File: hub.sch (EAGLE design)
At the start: 50 parts, among them U1 LM3526-L, X1 12MHz

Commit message: pick resistors
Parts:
- R1, R21, R24: DIGIKEY (none) -> 311-10.0KCRCT-ND; MPN (none) -> RC0805FR-0710KL; OC_MOUSER (none) -> 603-RC0805FR-0710KL
- R16: DIGIKEY (none) -> 311-47.0KCRCT-ND; MPN (none) -> RC0805FR-0747KL; OC_MOUSER (none) -> 603-RC0805FR-0747KL
- R2, R22, R23: DIGIKEY (none) -> 311-100KCRCT-ND; MPN (none) -> RC0805FR-07100KL; OC_MOUSER (none) -> 603-RC0805FR-07100KL
- R3: DIGIKEY (none) -> P649HCT-ND; MPN (none) -> ERJ-6ENF6490V; OC_MOUSER (none) -> 667-ERJ-6ENF6490V
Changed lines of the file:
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@@
 </part>
 <part name="SUPPLY1" library="supply2" library_urn="urn:adsk.eagle:library:372" deviceset="GND" device=""/>
-<part name="R1" library="rcl" library_urn="urn:adsk.eagle:library:334" deviceset="R-US_" device="M0805" package3d_urn="urn:adsk.eagle:package:23556/1" value="10K"/>
+<part name="R1" library="rcl" library_urn="urn:adsk.eagle:library:334" deviceset="R-US_" device="M0805" package3d_urn="urn:adsk.eagle:package:23556/1" value="10K">
+<attribute name="DIGIKEY" value="311-10.0KCRCT-ND"/>
+<attribute name="MPN" value="RC0805FR-0710KL"/>
+<attribute name="OC_MOUSER" value="603-RC0805FR-0710KL"/>
+</part>
 <part name="C13" library="rcl" library_urn="urn:adsk.eagle:library:334" deviceset="C-EU" device="C0805" package3d_urn="urn:adsk.eagle:package:23617/2" value="1uF"/>
-<part name="R16" library="rcl" library_urn="urn:adsk.eagle:library:334" deviceset="R-US_" device="M0805" package3d_urn="urn:adsk.eagle:package:23556/1" value="47K"/>
+<part name="R16" library="rcl" library_urn="urn:adsk.eagle:library:334" deviceset="R-US_" device="M0805" package3d_urn="urn:adsk.eagle:package:23556/1" value="47K">
+<attribute name="DIGIKEY" value="311-47.0KCRCT-ND"/>
+<attribute name="MPN" value="RC0805FR-0747KL"/>
+<attribute name="OC_MOUSER" value="603-RC0805FR-0747KL"/>
+</part>
 <part name="SUPPLY2" library="supply2" library_urn="urn:adsk.eagle:library:372" deviceset="GND" device=""/>
-<part name="R2" library="rcl" library_urn="urn:adsk.eagle:library:334" deviceset="R-US_" device="M0805" package3d_urn="urn:adsk.eagle:package:23556/1" value="100K"/>
+<part name="R2" library="rcl" library_urn="urn:adsk.eagle:library:334" deviceset="R-US_" device="M0805" package3d_urn="urn:adsk.eagle:package:23556/1" value="100K">
+<attribute name="DIGIKEY" value="311-100KCRCT-ND"/>
+<attribute name="MPN" value="RC0805FR-07100KL"/>
+<attribute name="OC_MOUSER" value="603-RC0805FR-07100KL"/>
+</part>
 <part name="SUPPLY3" library="supply2" library_urn="urn:adsk.eagle:library:372" deviceset="GND" device=""/>
-<part name="R3" library="rcl" library_urn="urn:adsk.eagle:library:334" deviceset="R-US_" device="M0805" package3d_urn="urn:adsk.eagle:package:23556/1" value="650R 1%"/>
+<part name="R3" library="rcl" library_urn="urn:adsk.eagle:library:334" deviceset="R-US_" device="M0805" package3d_urn="urn:adsk.eagle:package:23556/1" value="650R 1%">
+<attribute name="DIGIKEY" value="P649HCT-ND"/>
+<attribute name="MPN" value="ERJ-6ENF6490V"/>
+<attribute name="OC_MOUSER" value="667-ERJ-6ENF6490V"/>
+</part>
 <part name="SUPPLY4" library="supply2" library_urn="urn:adsk.eagle:library:372" deviceset="GND" device=""/>
 <part name="C14" library="rcl" library_urn="urn:adsk.eagle:library:334" deviceset="C-EU" device="C0805" package3d_urn="urn:adsk.eagle:package:23617/2" value="18P">
@@
 <part name="C17" library="rcl" library_urn="urn:adsk.eagle:library:334" deviceset="C-EU" device="C0805" package3d_urn="urn:adsk.eagle:package:23617/2" value="0.1uF"/>
 <part name="SUPPLY20" library="supply2" library_urn="urn:adsk.eagle:library:372" deviceset="GND" device=""/>
-<part name="R21" library="rcl" library_urn="urn:adsk.eagle:library:334" deviceset="R-US_" device="M0805" package3d_urn="urn:adsk.eagle:package:23556/1" value="10K"/>
-<part name="R22" library="rcl" library_urn="urn:adsk.eagle:library:334" deviceset="R-US_" device="M0805" package3d_urn="urn:adsk.eagle:package:23556/1" value="100K"/>
-<part name="R23" library="rcl" library_urn="urn:adsk.eagle:library:334" deviceset="R-US_" device="M0805" package3d_urn="urn:adsk.eagle:package:23556/1" value="100K"/>
-<part name="R24" library="rcl" library_urn="urn:adsk.eagle:library:334" deviceset="R-US_" device="M0805" package3d_urn="urn:adsk.eagle:package:23556/1" value="10K"/>
+<part name="R21" library="rcl" library_urn="urn:adsk.eagle:library:334" deviceset="R-US_" device="M0805" package3d_urn="urn:adsk.eagle:package:23556/1" value="10K">
+<attribute name="DIGIKEY" value="311-10.0KCRCT-ND"/>
+<attribute name="MPN" value="RC0805FR-0710KL"/>
+<attribute name="OC_MOUSER" value="603-RC0805FR-0710KL"/>
+</part>
+<part name="R22" library="rcl" library_urn="urn:adsk.eagle:library:334" deviceset="R-US_" device="M0805" package3d_urn="urn:adsk.eagle:package:23556/1" value="100K">
+<attribute name="DIGIKEY" value="311-100KCRCT-ND"/>
+<attribute name="MPN" value="RC0805FR-07100KL"/>
+<attribute name="OC_MOUSER" value="603-RC0805FR-07100KL"/>
+</part>
+<part name="R23" library="rcl" library_urn="urn:adsk.eagle:library:334" deviceset="R-US_" device="M0805" package3d_urn="urn:adsk.eagle:package:23556/1" value="100K">
+<attribute name="DIGIKEY" value="311-100KCRCT-ND"/>
+<attribute name="MPN" value="RC0805FR-07100KL"/>
+<attribute name="OC_MOUSER" value="603-RC0805FR-07100KL"/>
+</part>
+<part name="R24" library="rcl" library_urn="urn:adsk.eagle:library:334" deviceset="R-US_" device="M0805" package3d_urn="urn:adsk.eagle:package:23556/1" value="10K">
+<attribute name="DIGIKEY" value="311-10.0KCRCT-ND"/>
+<attribute name="MPN" value="RC0805FR-0710KL"/>
+<attribute name="OC_MOUSER" value="603-RC0805FR-0710KL"/>
+</part>
 <part name="TSUP3" library="sn65220_40" deviceset="SN65220" device="DBV">
 <attribute name="DIGIKEY" value="296-9694-1-ND"/>
@@
 </instance>
 <instance part="SUPPLY1" gate="GND" x="-15.24" y="-55.88"/>
-<instance part="R1" gate="G$1" x="66.04" y="-35.56" rot="R90"/>
+<instance part="R1" gate="G$1" x="66.04" y="-35.56" rot="R90">
+<attribute name="DIGIKEY" x="66.04" y="-35.56" size="1.778" layer="96" rot="R90" display="off"/>
+<attribute name="MPN" x="66.04" y="-35.56" size="1.778" layer="96" rot="R90" display="off"/>
+<attribute name="OC_MOUSER" x="66.04" y="-35.56" size="1.778" layer="96" rot="R90" display="off"/>
+</instance>
 <instance part="C13" gate="G$1" x="66.04" y="-53.34"/>
-<instance part="R16" gate="G$1" x="78.74" y="-55.88" rot="R90"/>
+<instance part="R16" gate="G$1" x="78.74" y="-55.88" rot="R90">
+<attribute name="DIGIKEY" x="78.74" y="-55.88" size="1.778" layer="96" rot="R90" display="off"/>
+<attribute name="MPN" x="78.74" y="-55.88" size="1.778" layer="96" rot="R90" display="off"/>
+<attribute name="OC_MOUSER" x="78.74" y="-55.88" size="1.778" layer="96" rot="R90" display="off"/>
+</instance>
 <instance part="SUPPLY2" gate="GND" x="66.04" y="-71.12"/>
-<instance part="R2" gate="G$1" x="101.6" y="-50.8"/>
+<instance part="R2" gate="G$1" x="101.6" y="-50.8">
+<attribute name="DIGIKEY" x="101.6" y="-50.8" size="1.778" layer="96" display="off"/>
+<attribute name="MPN" x="101.6" y="-50.8" size="1.778" layer="96" display="off"/>
+<attribute name="OC_MOUSER" x="101.6" y="-50.8" size="1.778" layer="96" display="off"/>
+</instance>
 <instance part="SUPPLY3" gate="GND" x="109.22" y="-60.96"/>
-<instance part="R3" gate="G$1" x="129.54" y="-45.72" rot="R90"/>
+<instance part="R3" gate="G$1" x="129.54" y="-45.72" rot="R90">
+<attribute name="DIGIKEY" x="129.54" y="-45.72" size="1.778" layer="96" rot="R90" display="off"/>
+<attribute name="MPN" x="129.54" y="-45.72" size="1.778" layer="96" rot="R90" display="off"/>
+<attribute name="OC_MOUSER" x="129.54" y="-45.72" size="1.778" layer="96" rot="R90" display="off"/>
+</instance>
 <instance part="SUPPLY4" gate="GND" x="129.54" y="-68.58"/>
 <instance part="C14" gate="G$1" x="157.48" y="-53.34">
@@
 <instance part="C17" gate="G$1" x="48.26" y="-86.36"/>
 <instance part="SUPPLY20" gate="GND" x="48.26" y="-99.06"/>
-<instance part="R21" gate="G$1" x="-43.18" y="-71.12" rot="R90"/>
-<instance part="R22" gate="G$1" x="-33.02" y="-71.12" rot="R90"/>
-<instance part="R23" gate="G$1" x="-22.86" y="-71.12" rot="R90"/>
-<instance part="R24" gate="G$1" x="-12.7" y="-71.12" rot="R90"/>
+<instance part="R21" gate="G$1" x="-43.18" y="-71.12" rot="R90">
+<attribute name="OC_MOUSER" x="-43.18" y="-71.12" size="1.778" layer="96" rot="R90" display="off"/>
+<attribute name="DIGIKEY" x="-43.18" y="-71.12" size="1.778" layer="96" rot="R90" display="off"/>
+<attribute name="MPN" x="-43.18" y="-71.12" size="1.778" layer="96" rot="R90" display="off"/>
+</instance>
+<instance part="R22" gate="G$1" x="-33.02" y="-71.12" rot="R90">
+<attribute name="MPN" x="-33.02" y="-71.12" size="1.778" layer="96" rot="R90" display="off"/>
+<attribute name="DIGIKEY" x="-33.02" y="-71.12" size="1.778" layer="96" rot="R90" display="off"/>
+<attribute name="OC_MOUSER" x="-33.02" y="-71.12" size="1.778" layer="96" rot="R90" display="off"/>
+</instance>
+<instance part="R23" gate="G$1" x="-22.86" y="-71.12" rot="R90">
+<attribute name="MPN" x="-22.86" y="-71.12" size="1.778" layer="96" rot="R90" display="off"/>
+<attribute name="DIGIKEY" x="-22.86" y="-71.12" size="1.778" layer="96" rot="R90" display="off"/>
+<attribute name="OC_MOUSER" x="-22.86" y="-71.12" size="1.778" layer="96" rot="R90" display="off"/>
+</instance>
+<instance part="R24" gate="G$1" x="-12.7" y="-71.12" rot="R90">
+<attribute name="OC_MOUSER" x="-12.7" y="-71.12" size="1.778" layer="96" rot="R90" display="off"/>
+<attribute name="DIGIKEY" x="-12.7" y="-71.12" size="1.778" layer="96" rot="R90" display="off"/>
+<attribute name="MPN" x="-12.7" y="-71.12" size="1.778" layer="96" rot="R90" display="off"/>
+</instance>
 <instance part="TSUP3" gate="G$1" x="45.72" y="53.34" rot="R90">
 <attribute name="DIGIKEY" x="45.72" y="53.34" size="1.778" layer="96" rot="R90" display="off"/>

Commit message: pick capacitors
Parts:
- C1, C10, C11, C12, C16, C17, C19, C20, C21, C22, C4, C8, C9: DIGIKEY (none) -> 490-1666-1-ND; MPN (none) -> GRM21BR71H104KA01L; OC_MOUSER (none) -> 81-GRM40X104K50L
- C13, C2, C3, C5: DIGIKEY (none) -> 399-1284-1-ND; MPN (none) -> C0805C105K4RACTU; OC_MOUSER (none) -> 80-C0805C105K4R

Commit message: complete BOM
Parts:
- C14, C15: MPN (none) -> CL10C180JB8NNNC
- LB1, LB6: value (none) -> 220; DIGIKEY (none) -> 490-1054-1-ND; MPN (none) -> BLM21PG221SN1D; OC_MOUSER (none) -> 81-BLM21P221SG
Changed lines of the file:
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@@
 <part name="C14" library="rcl" library_urn="urn:adsk.eagle:library:334" deviceset="C-EU" device="C0805" package3d_urn="urn:adsk.eagle:package:23617/2" value="18P">
 <attribute name="DIGIKEY" value="1276-1089-1-ND"/>
+<attribute name="MPN" value="CL10C180JB8NNNC"/>
 <attribute name="OC_MOUSER" value="77-VJ0603A180JXACBC"/>
 </part>
 <part name="C15" library="rcl" library_urn="urn:adsk.eagle:library:334" deviceset="C-EU" device="C0805" package3d_urn="urn:adsk.eagle:package:23617/2" value="18P">
 <attribute name="DIGIKEY" value="1276-1089-1-ND"/>
+<attribute name="MPN" value="CL10C180JB8NNNC"/>
 <attribute name="OC_MOUSER" value="77-VJ0603A180JXACBC"/>
 </part>
@@
 <part name="SUPPLY23" library="supply2" library_urn="urn:adsk.eagle:library:372" deviceset="GND" device=""/>
 <part name="SUPPLY24" library="supply2" library_urn="urn:adsk.eagle:library:372" deviceset="GND" device=""/>
-<part name="LB1" library="rcl" library_urn="urn:adsk.eagle:library:334" deviceset="R-EU_" device="R0805" package3d_urn="urn:adsk.eagle:package:23553/2"/>
+<part name="LB1" library="rcl" library_urn="urn:adsk.eagle:library:334" deviceset="R-EU_" device="R0805" package3d_urn="urn:adsk.eagle:package:23553/2" value="220">
+<attribute name="DIGIKEY" value="490-1054-1-ND"/>
+<attribute name="MPN" value="BLM21PG221SN1D"/>
+<attribute name="OC_MOUSER" value="81-BLM21P221SG"/>
+</part>
 <part name="+3V3_1" library="supply1" library_urn="urn:adsk.eagle:library:371" deviceset="+3V3" device=""/>
 <part name="+3V3_4" library="supply1" library_urn="urn:adsk.eagle:library:371" deviceset="+3V3" device=""/>
@@
 <part name="P+1" library="supply1" library_urn="urn:adsk.eagle:library:371" deviceset="V+" device=""/>
 <part name="P+2" library="supply1" library_urn="urn:adsk.eagle:library:371" deviceset="V+" device=""/>
-<part name="LB6" library="rcl" library_urn="urn:adsk.eagle:library:334" deviceset="R-EU_" device="R0805" package3d_urn="urn:adsk.eagle:package:23553/2"/>
+<part name="LB6" library="rcl" library_urn="urn:adsk.eagle:library:334" deviceset="R-EU_" device="R0805" package3d_urn="urn:adsk.eagle:package:23553/2" value="220">
+<attribute name="DIGIKEY" value="490-1054-1-ND"/>
+<attribute name="MPN" value="BLM21PG221SN1D"/>
+<attribute name="OC_MOUSER" value="81-BLM21P221SG"/>
+</part>
 <part name="SUPPLY26" library="supply2" library_urn="urn:adsk.eagle:library:372" deviceset="GND" device=""/>
 <part name="J3" library="InputOutputIO (rev17e)" deviceset="61400826021" device="">
@@
 <attribute name="DIGIKEY" x="157.48" y="-53.34" size="1.778" layer="96" display="off"/>
 <attribute name="OC_MOUSER" x="157.48" y="-53.34" size="1.778" layer="96" display="off"/>
+<attribute name="MPN" x="157.48" y="-53.34" size="1.778" layer="96" display="off"/>
 </instance>
 <instance part="C15" gate="G$1" x="193.04" y="-53.34">
 <attribute name="DIGIKEY" x="193.04" y="-53.34" size="1.778" layer="96" display="off"/>
 <attribute name="OC_MOUSER" x="193.04" y="-53.34" size="1.778" layer="96" display="off"/>
+<attribute name="MPN" x="193.04" y="-53.34" size="1.778" layer="96" display="off"/>
 </instance>
 <instance part="SUPPLY5" gate="GND" x="157.48" y="-68.58"/>
@@
 <instance part="SUPPLY23" gate="GND" x="43.18" y="40.64"/>
 <instance part="SUPPLY24" gate="GND" x="38.1" y="73.66"/>
-<instance part="LB1" gate="G$1" x="63.5" y="73.66"/>
+<instance part="LB1" gate="G$1" x="63.5" y="73.66">
+<attribute name="MPN" x="63.5" y="73.66" size="1.778" layer="96" display="off"/>
+<attribute name="DIGIKEY" x="63.5" y="73.66" size="1.778" layer="96" display="off"/>
+<attribute name="OC_MOUSER" x="63.5" y="73.66" size="1.778" layer="96" display="off"/>
+</instance>
 <instance part="+3V3_1" gate="G$1" x="68.58" y="48.26"/>
 <instance part="+3V3_4" gate="G$1" x="149.86" y="93.98"/>
@@
 <instance part="P+1" gate="1" x="86.36" y="48.26"/>
 <instance part="P+2" gate="1" x="114.3" y="48.26"/>
-<instance part="LB6" gate="G$1" x="78.74" y="30.48"/>
+<instance part="LB6" gate="G$1" x="78.74" y="30.48">
+<attribute name="MPN" x="78.74" y="30.48" size="1.778" layer="96" display="off"/>
+<attribute name="DIGIKEY" x="78.74" y="30.48" size="1.778" layer="96" display="off"/>
+<attribute name="OC_MOUSER" x="78.74" y="30.48" size="1.778" layer="96" display="off"/>
+</instance>
 <instance part="SUPPLY26" gate="GND" x="48.26" y="-10.16" rot="R90"/>
 <instance part="J3" gate="G$1" x="236.22" y="-48.26" rot="R270">

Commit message: finish pin-strapping
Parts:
- added R5, R6: 10K, rcl:R-US_M0805
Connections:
- removed net NOVRP3: U$1.OVR#[3]
- removed net NOVRP4: U$1.OVR#[4]
- new net N$6: R6.2, U$1.GREEN[4]
- new net N$7: R5.2, U$1.GREEN[3]
- net +3V3: now also R5.1, R6.1, U$1.OVR#[3], U$1.OVR#[4]

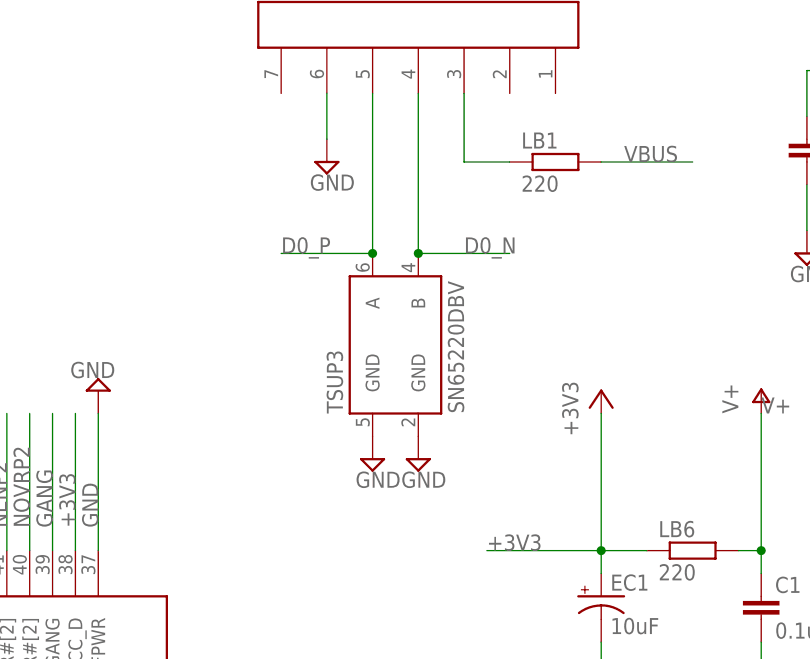
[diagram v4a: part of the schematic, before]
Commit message: re-route USB for oshpark PCBs
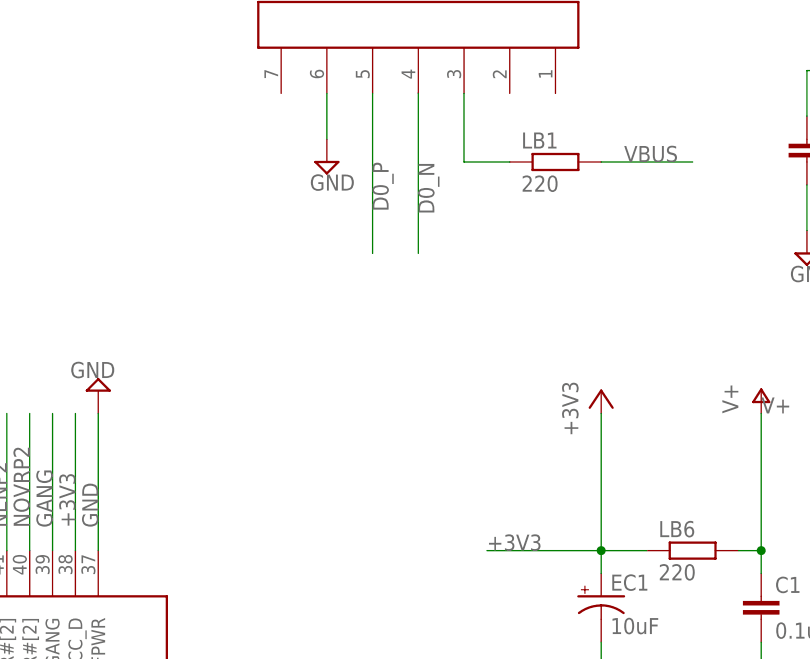
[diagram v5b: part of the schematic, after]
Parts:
- removed TSUP3: SN65220DBV, sn65220_40:SN65220DBV
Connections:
- net D0_N: no longer TSUP3.B
- net D0_P: no longer TSUP3.A
- net GND: no longer TSUP3.GND@1, TSUP3.GND@2
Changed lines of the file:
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@@
 <attribute name="OC_MOUSER" value="603-RC0805FR-0710KL"/>
 </part>
-<part name="TSUP3" library="sn65220_40" deviceset="SN65220" device="DBV">
-<attribute name="DIGIKEY" value="296-9694-1-ND"/>
-<attribute name="MPN" value="SN65220DBVR"/>
-<attribute name="OC_MOUSER" value="595-SN65220DBVR"/>
-</part>
-<part name="SUPPLY22" library="supply2" library_urn="urn:adsk.eagle:library:372" deviceset="GND" device=""/>
-<part name="SUPPLY23" library="supply2" library_urn="urn:adsk.eagle:library:372" deviceset="GND" device=""/>
 <part name="SUPPLY24" library="supply2" library_urn="urn:adsk.eagle:library:372" deviceset="GND" device=""/>
 <part name="LB1" library="rcl" library_urn="urn:adsk.eagle:library:334" deviceset="R-EU_" device="R0805" package3d_urn="urn:adsk.eagle:package:23553/2" value="220">
@@
 <attribute name="MPN" x="-12.7" y="-71.12" size="1.778" layer="96" rot="R90" display="off"/>
 </instance>
-<instance part="TSUP3" gate="G$1" x="45.72" y="53.34" rot="R90">
-<attribute name="DIGIKEY" x="45.72" y="53.34" size="1.778" layer="96" rot="R90" display="off"/>
-<attribute name="MPN" x="45.72" y="53.34" size="1.778" layer="96" rot="R90" display="off"/>
-<attribute name="OC_MOUSER" x="45.72" y="53.34" size="1.778" layer="96" rot="R90" display="off"/>
-</instance>
-<instance part="SUPPLY22" gate="GND" x="48.26" y="40.64"/>
-<instance part="SUPPLY23" gate="GND" x="43.18" y="40.64"/>
 <instance part="SUPPLY24" gate="GND" x="38.1" y="73.66"/>
 <instance part="LB1" gate="G$1" x="63.5" y="73.66">
@@
 </segment>
 <segment>
-<pinref part="TSUP3" gate="G$1" pin="GND@2"/>
-<pinref part="SUPPLY22" gate="GND" pin="GND"/>
-</segment>
-<segment>
-<pinref part="TSUP3" gate="G$1" pin="GND@1"/>
-<pinref part="SUPPLY23" gate="GND" pin="GND"/>
-</segment>
-<segment>
 <pinref part="U$1" gate="G$1" pin="SELFPWR"/>
 <wire x1="12.7" y1="30.48" x2="12.7" y2="45.72" width="0.1524" layer="91"/>
@@
 </segment>
 <segment>
-<pinref part="TSUP3" gate="G$1" pin="B"/>
-<wire x1="48.26" y1="63.5" x2="58.42" y2="63.5" width="0.1524" layer="91"/>
-<label x="53.34" y="63.5" size="1.778" layer="95"/>
+<label x="48.26" y="73.66" size="1.778" layer="95" rot="R270"/>
 <pinref part="J2" gate="G$1" pin="4"/>
 <wire x1="48.26" y1="81.28" x2="48.26" y2="63.5" width="0.1524" layer="91"/>
-<junction x="48.26" y="63.5"/>
 </segment>
 </net>
@@
 </segment>
 <segment>
-<pinref part="TSUP3" gate="G$1" pin="A"/>
-<wire x1="43.18" y1="63.5" x2="33.02" y2="63.5" width="0.1524" layer="91"/>
-<label x="33.02" y="63.5" size="1.778" layer="95"/>
+<label x="43.18" y="73.66" size="1.778" layer="95" rot="R270"/>
 <pinref part="J2" gate="G$1" pin="5"/>
 <wire x1="43.18" y1="81.28" x2="43.18" y2="63.5" width="0.1524" layer="91"/>
-<junction x="43.18" y="63.5"/>
 </segment>
 </net>
